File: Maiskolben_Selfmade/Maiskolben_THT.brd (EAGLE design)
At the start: 72.2 x 80.8 mm, 33 parts, among them IC1 OPA703PA, J2 AUDIO_JACK_5PEBS_35, Q1 IRF5305, Q2 2N7000, U1 CD4050DIP16, U2 ARDUINO_NANOR3

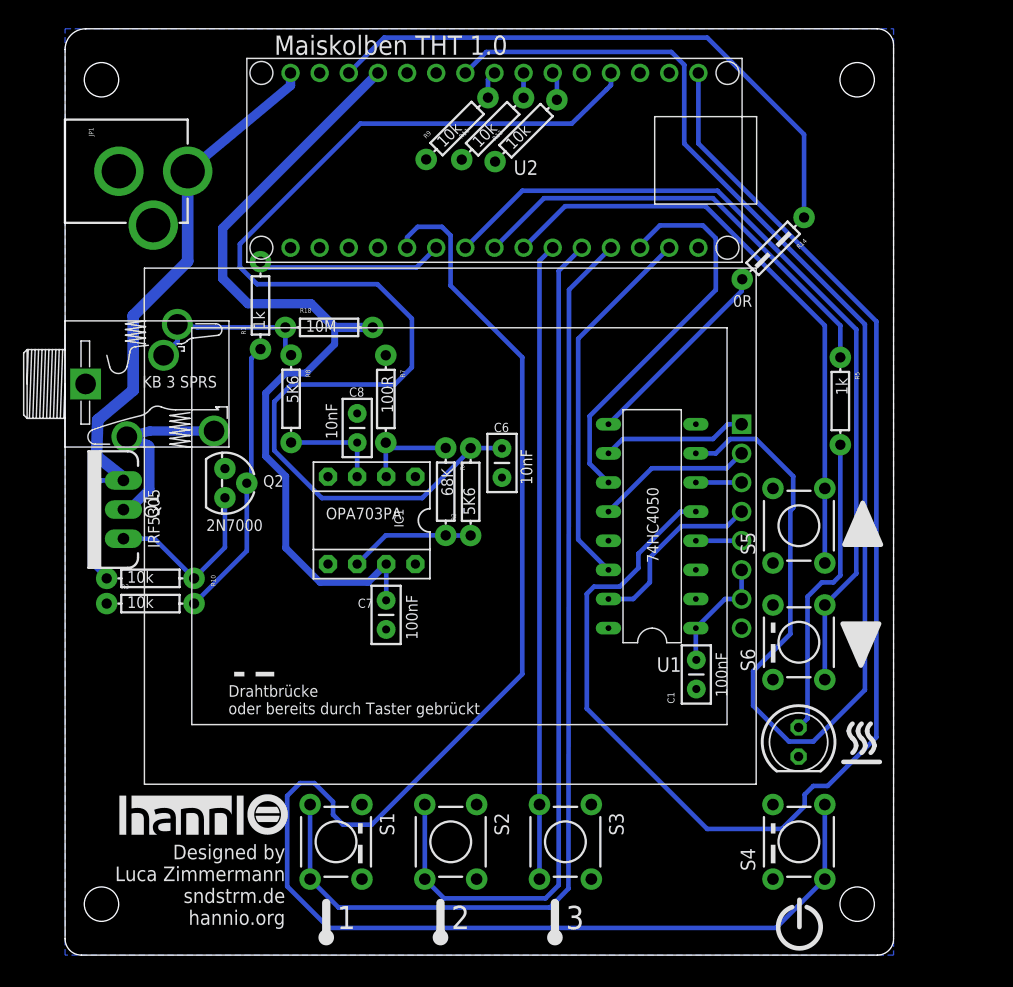
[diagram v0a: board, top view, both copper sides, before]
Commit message: Fixed 3v3 connection
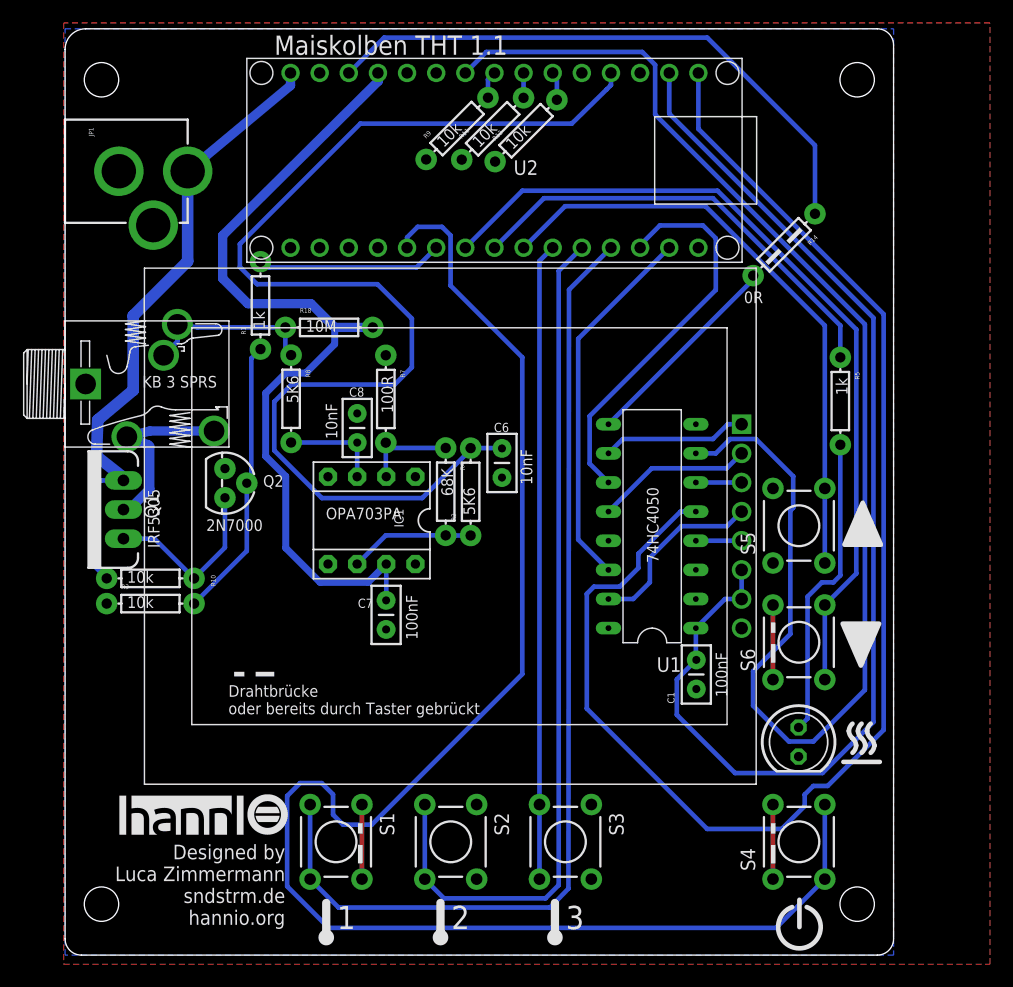
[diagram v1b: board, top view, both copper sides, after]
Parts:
- moved R14 1.00 mm to (62.7, 61.9)
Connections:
- removed net 3V3: U2.3V3
- net 3.3V: now also U2.3V3
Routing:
- net 3.3V: track 10.4 -> 100.9 mm
- net DGND: track 0.00 -> 19.5 mm
- net DC: track 126.0 -> 124.6 mm
- net RESET_R: track 17.5 -> 18.2 mm
- net SCK: track 121.1 -> 121.6 mm
- added copper zone on layer 1, net DGND
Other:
- board text added: "Maiskolben THT 1.1"
- board text removed: "Maiskolben THT 1.0"
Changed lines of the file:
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@@
 <setting verticaltext="up"/>
 </settings>
-<grid distance="1.27" unitdist="mm" unit="mm" style="dots" multiple="1" display="yes" altdistance="0.0125" altunitdist="inch" altunit="inch"/>
+<grid distance="12.5" unitdist="mil" unit="mil" style="dots" multiple="1" display="yes" altdistance="0.0125" altunitdist="inch" altunit="inch"/>
 <layers>
 <layer number="1" name="Top" color="4" fill="1" visible="yes" active="yes"/>
@@
 <layer number="39" name="tKeepout" color="4" fill="11" visible="no" active="yes"/>
 <layer number="40" name="bKeepout" color="1" fill="11" visible="no" active="yes"/>
-<layer number="41" name="tRestrict" color="4" fill="10" visible="no" active="yes"/>
+<layer number="41" name="tRestrict" color="4" fill="10" visible="yes" active="yes"/>
 <layer number="42" name="bRestrict" color="1" fill="10" visible="yes" active="yes"/>
 <layer number="43" name="vRestrict" color="2" fill="10" visible="no" active="yes"/>
@@
 <wire x1="70.2451" y1="18.9097" x2="69.9276" y2="19.5447" width="0.4064" layer="21" curve="-45"/>
 <wire x1="70.2451" y1="20.1797" x2="69.9276" y2="19.5447" width="0.4064" layer="21" curve="45"/>
-<circle x="52.3045" y="11.43" radius="4.879178125" width="0.4064" layer="41"/>
 <text x="35.56" y="56.7055" size="0.4064" layer="126" rot="MR90" align="center">AUTORESET</text>
 <text x="33.42" y="54.920996875" size="0.799996875" layer="126" ratio="15" rot="MR270" align="center">C1</text>
@@
 <wire x1="61.739" y1="8" x2="61.739" y2="11.5" width="0.4064" layer="21" style="shortdash"/>
 <wire x1="61.739" y1="25.5" x2="61.739" y2="29" width="0.4064" layer="21" style="shortdash"/>
-<wire x1="60.239" y1="60" x2="63.239" y2="63" width="0.4064" layer="21" style="shortdash"/>
-<text x="18.239" y="78.5" size="1.6764" layer="21" ratio="12">Maiskolben THT 1.0</text>
+<wire x1="61.1915" y1="60.3175" x2="64.1915" y2="63.3175" width="0.4064" layer="21" style="shortdash"/>
+<text x="18.239" y="78.5" size="1.6764" layer="21" ratio="12">Maiskolben THT 1.1</text>
 <text x="14.239" y="21" size="1.016" layer="21">Drahtbrücke
 oder bereits durch Taster gebrückt</text>
@@
 </element>
 <element name="J2" library="rgb_matrix" package="EBS_35" value="AUDIO_JACK_5PEBS_35" x="-3.611" y="49.8"/>
-<element name="R14" library="SparkFun-Resistors" package="AXIAL-0.3" value="0R" x="61.739" y="61.625" smashed="yes" rot="R225">
-<attribute name="NAME" x="64.433078125" y="62.523025" size="0.4064" layer="25" font="vector" rot="R225"/>
-<attribute name="VALUE" x="58.239934375" y="56.5306125" size="1.016" layer="21" font="vector" ratio="15"/>
+<element name="R14" library="SparkFun-Resistors" package="AXIAL-0.3" value="0R" x="62.6915" y="61.9425" smashed="yes" rot="R225">
+<attribute name="NAME" x="65.385578125" y="62.840525" size="0.4064" layer="25" font="vector" rot="R225"/>
+<attribute name="VALUE" x="59.192434375" y="56.8481125" size="1.016" layer="21" font="vector" ratio="15"/>
 </element>
 <element name="U$1" library="rgb_matrix" package="HANNIO_MEDIUM" value="HANNIO_MEDIUM" x="4.739" y="10.5"/>
@@
 <contactref element="R11" pad="P$1"/>
 <contactref element="R9" pad="P$1"/>
-<wire x1="61.7234" y1="13.1312" x2="61.7234" y2="6.6288" width="0" layer="19" extent="1-1"/>
-<wire x1="61.7234" y1="24.0278" x2="58.989" y2="28.51" width="0" layer="19" extent="1-1"/>
-<wire x1="25.8856" y1="13.1312" x2="25.8856" y2="6.6288" width="0" layer="19" extent="1-1"/>
+<wire x1="61.7234" y1="24.0278" x2="61.7234" y2="30.5302" width="0.4064" layer="1"/>
+<wire x1="25.8856" y1="6.6288" x2="25.8856" y2="13.1312" width="0.4064" layer="1"/>
+<wire x1="61.7234" y1="6.6288" x2="61.7234" y2="13.1312" width="0.4064" layer="1"/>
+<polygon width="0.4064" layer="1">
+<vertex x="80.645" y="-0.8015"/>
+<vertex x="80.645" y="81.28"/>
+<vertex x="-0.125" y="81.28"/>
+<vertex x="-0.125" y="-0.8015"/>
+</polygon>
 </signal>
 <signal name="+5V">
@@
 <wire x1="21.439" y1="56.8" x2="23.507" y2="54.732" width="0.8128" layer="16"/>
 <wire x1="23.507" y1="54.732" x2="26.829" y2="54.732" width="0.8128" layer="16"/>
-<wire x1="13.739" y1="59" x2="13.739" y2="63.38" width="0.8128" layer="16"/>
-<wire x1="13.739" y1="63.38" x2="27.279" y2="76.92" width="0.8128" layer="16"/>
+<wire x1="13.739" y1="59" x2="13.739" y2="62.745" width="0.8128" layer="16"/>
+<wire x1="13.739" y1="62.745" x2="27.305" y2="76.2" width="0.8128" layer="16"/>
+<wire x1="27.305" y1="76.2" x2="27.305" y2="76.92" width="0.8128" layer="16"/>
+<wire x1="27.305" y1="76.92" x2="27.279" y2="76.92" width="0.8128" layer="16"/>
 <wire x1="28.0045" y1="34.097" x2="26.4075" y2="32.5" width="0.6096" layer="16"/>
 <wire x1="26.4075" y1="32.5" x2="22.239" y2="32.5" width="0.6096" layer="16"/>
@@
 <wire x1="55.989" y1="80" x2="27.819" y2="80" width="0.4064" layer="16"/>
 <wire x1="27.819" y1="80" x2="24.739" y2="76.92" width="0.4064" layer="16"/>
-<wire x1="64.433075" y1="64.319075" x2="64.433078125" y2="71.555921875" width="0.4064" layer="16"/>
-<wire x1="64.433078125" y1="71.555921875" x2="55.989" y2="80" width="0.4064" layer="16"/>
+<wire x1="65.385575" y1="64.636575" x2="65.385578125" y2="70.603421875" width="0.4064" layer="16"/>
+<wire x1="65.385578125" y1="70.603421875" x2="55.989" y2="80" width="0.4064" layer="16"/>
 </signal>
 <signal name="HEATER_PWM">
@@
 <wire x1="64.489" y1="14" x2="65.239" y2="14.75" width="0.4064" layer="16"/>
 <wire x1="65.239" y1="14.75" x2="66.489" y2="14.75" width="0.4064" layer="16"/>
-<wire x1="66.489" y1="14.75" x2="70.739" y2="19" width="0.4064" layer="16"/>
-<wire x1="55.219" y1="76.92" x2="55.219" y2="70.77" width="0.4064" layer="16"/>
-<wire x1="55.219" y1="70.77" x2="70.739" y2="55.25" width="0.4064" layer="16"/>
-<wire x1="70.739" y1="55.25" x2="70.739" y2="19" width="0.4064" layer="16"/>
+<wire x1="66.489" y1="14.75" x2="71.374" y2="19.635" width="0.4064" layer="16"/>
+<wire x1="55.219" y1="76.92" x2="55.219" y2="72.04" width="0.4064" layer="16"/>
+<wire x1="55.219" y1="72.04" x2="71.374" y2="55.885" width="0.4064" layer="16"/>
+<wire x1="71.374" y1="55.885" x2="71.374" y2="19.635" width="0.4064" layer="16"/>
 </signal>
 <signal name="TEMP">
@@
 <wire x1="65.239" y1="18.625" x2="69.739" y2="23.125" width="0.4064" layer="16"/>
 <wire x1="69.739" y1="23.125" x2="69.739" y2="55" width="0.4064" layer="16"/>
-<wire x1="69.739" y1="55" x2="53.989" y2="70.75" width="0.4064" layer="16"/>
-<wire x1="36.729" y1="78.75" x2="52.864" y2="78.75" width="0.4064" layer="16"/>
-<wire x1="52.864" y1="78.75" x2="53.989" y2="77.625" width="0.4064" layer="16"/>
-<wire x1="53.989" y1="77.625" x2="53.989" y2="70.75" width="0.4064" layer="16"/>
+<wire x1="69.739" y1="55" x2="51.449" y2="73.29" width="0.4064" layer="16"/>
+<wire x1="36.729" y1="78.75" x2="50.324" y2="78.75" width="0.4064" layer="16"/>
+<wire x1="50.324" y1="78.75" x2="51.449" y2="77.625" width="0.4064" layer="16"/>
+<wire x1="51.449" y1="77.625" x2="51.449" y2="73.29" width="0.4064" layer="16"/>
 </signal>
 <signal name="STBY_NO">
@@
 <wire x1="54.999" y1="28.51" x2="54.999" y2="25.78" width="0.4064" layer="16"/>
 <wire x1="54.999" y1="25.78" x2="55.039" y2="25.74" width="0.4064" layer="16"/>
+<contactref element="U2" pad="3V3"/>
+<wire x1="52.679" y1="76.92" x2="52.679" y2="73.3685" width="0.4064" layer="16"/>
+<wire x1="52.679" y1="73.3685" x2="70.485" y2="55.5625" width="0.4064" layer="16"/>
+<wire x1="70.485" y1="55.5625" x2="70.485" y2="20.32" width="0.4064" layer="16"/>
+<wire x1="70.485" y1="20.32" x2="66.04" y2="15.875" width="0.4064" layer="16"/>
+<wire x1="66.04" y1="15.875" x2="58.42" y2="15.875" width="0.4064" layer="16"/>
+<wire x1="58.42" y1="15.875" x2="53.34" y2="20.955" width="0.4064" layer="16"/>
+<wire x1="53.34" y1="20.955" x2="53.34" y2="24.041" width="0.4064" layer="16"/>
+<wire x1="53.34" y1="24.041" x2="55.039" y2="25.74" width="0.4064" layer="16"/>
 </signal>
 <signal name="TFT_RESET">
@@
 <wire x1="61.9908" y1="2.375" x2="66.2446" y2="6.6288" width="0.4064" layer="16"/>
 <wire x1="19.364" y1="13.875" x2="20.489" y2="15" width="0.4064" layer="16"/>
-<wire x1="20.489" y1="15" x2="21.739" y2="15" width="0.4064" layer="16"/>
-<wire x1="21.739" y1="15" x2="23.364" y2="13.375" width="0.4064" layer="16"/>
-<wire x1="23.364" y1="13.375" x2="23.364" y2="12.25" width="0.4064" layer="16"/>
+<wire x1="20.489" y1="15" x2="22.374" y2="15" width="0.4064" layer="16"/>
+<wire x1="22.374" y1="15" x2="23.364" y2="14.01" width="0.4064" layer="16"/>
+<wire x1="23.364" y1="14.01" x2="23.364" y2="12.25" width="0.4064" layer="16"/>
 <wire x1="23.364" y1="12.25" x2="24.239" y2="11.375" width="0.4064" layer="16"/>
 <wire x1="24.239" y1="11.375" x2="26.739" y2="11.375" width="0.4064" layer="16"/>
@@
 <wire x1="50.139" y1="61.9" x2="50.139" y2="61.68" width="0.4064" layer="16"/>
 </signal>
-<signal name="3V3">
-<contactref element="U2" pad="3V3"/>
-</signal>
 <signal name="N$3">
 <contactref element="Q2" pad="2"/>
@@
 <contactref element="R14" pad="P$2"/>
 <contactref element="U1" pad="IN_D"/>
-<wire x1="47.379" y1="46.29" x2="58.989" y2="57.9" width="0.4064" layer="16"/>
-<wire x1="58.989" y1="57.9" x2="59.044921875" y2="58.930921875" width="0.4064" layer="16"/>
+<wire x1="47.379" y1="46.29" x2="59.9415" y2="58.8525" width="0.4064" layer="16"/>
+<wire x1="59.9415" y1="58.8525" x2="59.997421875" y2="59.248421875" width="0.4064" layer="16"/>
 </signal>
 </signals>
